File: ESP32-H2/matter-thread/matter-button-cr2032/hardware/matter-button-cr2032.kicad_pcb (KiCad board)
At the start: 2 copper layers, 30 x 38 mm, 37 parts, among them Q1 DMG2305UX, SW1 PTS810, U1 ESP32-H2-WROOM-02C-H4S, U2 TPS63900DSKR

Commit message: matter-button-cr2032: JLCPCB Basic parts and LCSC part numbers
Every assembled part now carries an LCSC part number (schematic field,
footprint field, BOM). Common parts moved to the JLCPCB Basic library:
- Q1 AO3401A (C15127) instead of DMG2305UX, same SOT-23 pinout
- D1 KT-0603R (C2286), passives UNI-ROYAL / Samsung Basic parts
- R3 (CFG3) 0 ohm as the TI 3.3 V reference design: VO(1) = 1.8 V,
  unused because SEL is tied to VIN; R2 and R3 share one part
- R6 button pull-up 1 Mohm (same part as R9): 3.3 uA while pressed
Extended parts left: U2, L1 (DFE252012P-2R2M), C1/C2, R1 36.5k, SW1
(PTS810 SJM, 160 gf). U1 and BT1 are not stocked by LCSC: left out of
the JLCPCB BOM and CPL, hand soldered.

gen_pcb.py sync updates values and part fields on the routed board
without placement or routing. Copper and Gerbers are unchanged;
ERC 0, DRC 0 with schematic parity.

Co-Authored-By: Claude Opus 5.5 <noreply@anthropic.com>
Claude-Session: https://claude.ai/code/session_01R15P3zWK2KCijMWrCL7LHn
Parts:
- Q1: value DMG2305UX -> AO3401A
- R3: value 16.2k -> 0R
- R6: value 470k -> 1M

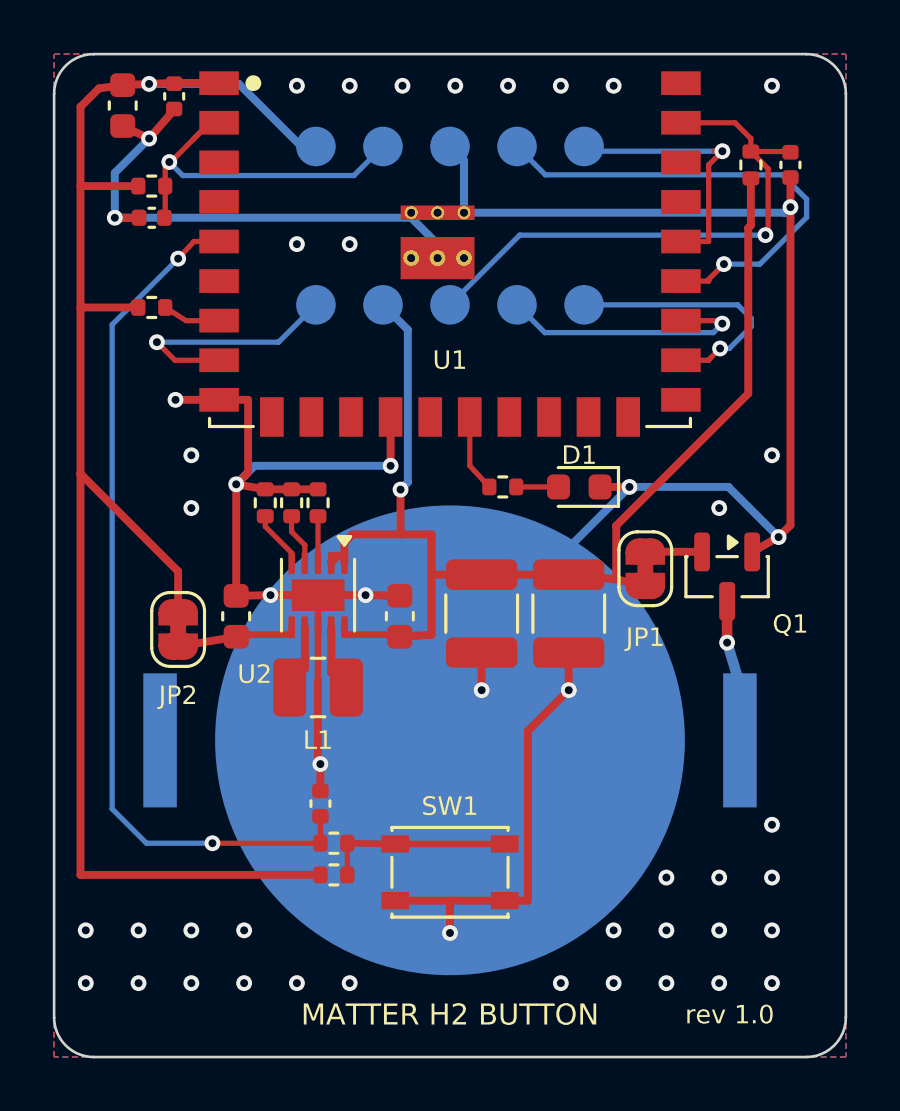
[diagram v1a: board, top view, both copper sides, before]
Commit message: matter-button-cr2032: compact 25 x 27 mm PCB
Same schematic, new layout: the CR2032 holder moves under the module and
the circuit, the board shrinks from 30 x 38 to 25 x 27 mm (41 % less area).
- the holder (23.2 mm between its tab ends) sets the width; the cell edge
  is now 6.5 mm from the antenna feed (was ~16 mm), the docs ask for an
  RSSI/LQI check and point to the previous layout as fallback
- bottom side: no copper in a ring around the cell edge (the + can), GND
  vias only inside the contact pad or outside the cell
- test pads stay on the bottom side under the module (2 x 5, 2.54 x 2.7 mm)
- gen_pcb.py: new placement and hand routes, coin-cell ring rule areas,
  duplicate segment cleanup, saving the board keeps the project file
ERC 0, DRC 0 with schematic parity.

Co-Authored-By: Claude Opus 5.5 <noreply@anthropic.com>
Claude-Session: https://claude.ai/code/session_01R15P3zWK2KCijMWrCL7LHn
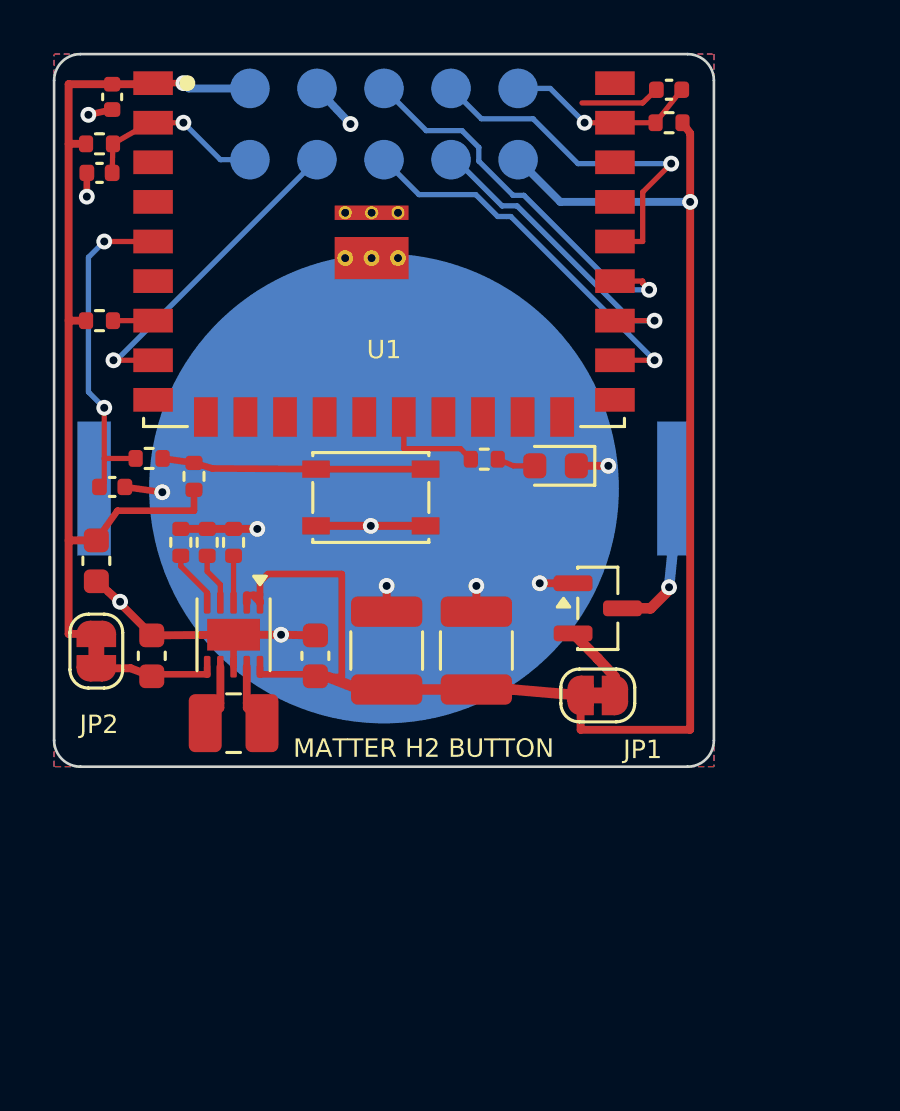
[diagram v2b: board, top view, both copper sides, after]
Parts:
- moved C5 17.3 mm to (101.6, 119.2)
- moved R7 16.2 mm to (103.6, 115.3)
- moved R6 16.0 mm to (105.3, 116.0), turned to 90 degrees
- moved SW1 14.5 mm to (112.0, 116.8)
- moved C8 14.4 mm to (102.2, 116.4), turned to 0 degrees
- moved BT1 9.86 mm to (112.5, 116.5)
- moved TP4 9.37 mm to (112.5, 104.0)
- moved TP10 8.60 mm to (117.6, 101.3)
- moved TP9 7.51 mm to (117.6, 104.0)
- moved C2 7.04 mm to (112.6, 122.6), turned to 90 degrees
- moved TP3 6.04 mm to (115.0, 104.0)
- moved TP6 5.50 mm to (110.0, 104.0)
- moved TP2 5.50 mm to (110.0, 101.3)
- moved TP7 5.50 mm to (112.5, 101.3)
- moved TP8 5.50 mm to (115.0, 101.3)
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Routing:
- net GND: track 137.8 -> 34.7 mm, vias 51 -> 12
- net +3V3: track 62.2 -> 36.3 mm
- net /BTN: track 33.2 -> 12.9 mm
- net /VBAT_SENSE: track 21.4 -> 6.69 mm
- net VBAT: track 47.8 -> 57.7 mm
- net /EN: track 13.9 -> 7.13 mm
- net /RXD0: track 10.1 -> 14.9 mm
- net /USB_DN: track 18.3 -> 15.0 mm
- net /BOOT: track 9.25 -> 12.4 mm
- net /BTN_SW: track 7.17 -> 10.0 mm
- net /USB_DP: track 11.2 -> 14.0 mm
- net /TXD0: track 9.97 -> 11.7 mm
- net /LED: track 2.94 -> 3.91 mm
- net /VBAT_Q: track 2.16 -> 2.99 mm
- net /LX2: track 1.59 -> 2.38 mm
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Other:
- board size 30 x 38 mm -> 25 x 27 mm
- board text removed: "CR2032 +"

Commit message: matter-button-cr2032: 29.8 x 23.9 mm PCB, under 30 x 30 mm with the antenna
Same schematic, new layout so the whole board including the module antenna
overhang fits in 30 x 30 mm (29.8 x 29.9 mm), no mounting holes.
- module at the top right edge, passives and the TPS63900 on its left,
  button in the middle, battery input and sense on the right
- the cell edge is now 3.4 mm from the antenna base (25 x 27 mm: 6.5 mm);
  the docs ask for an RSSI/LQI check and point to the earlier layouts
- test pads: 2 x 2 in each top corner, RX and VBAT right of the holder;
  every signal is routed in the script, so the route stage skips
  FreeRouting when only GND (the pours) is left
- silkscreen: "Thread Button" (top), "Made by Haxeko" (bottom), JP1 label
- place no longer leaves the project file rewritten with KiCad defaults
  (NewBoard writes it before the save), 3D renders in landscape
ERC 0, DRC 0 with schematic parity; BOM unchanged.

Co-Authored-By: Claude Opus 5.5 <noreply@anthropic.com>
Claude-Session: https://claude.ai/code/session_01R15P3zWK2KCijMWrCL7LHn
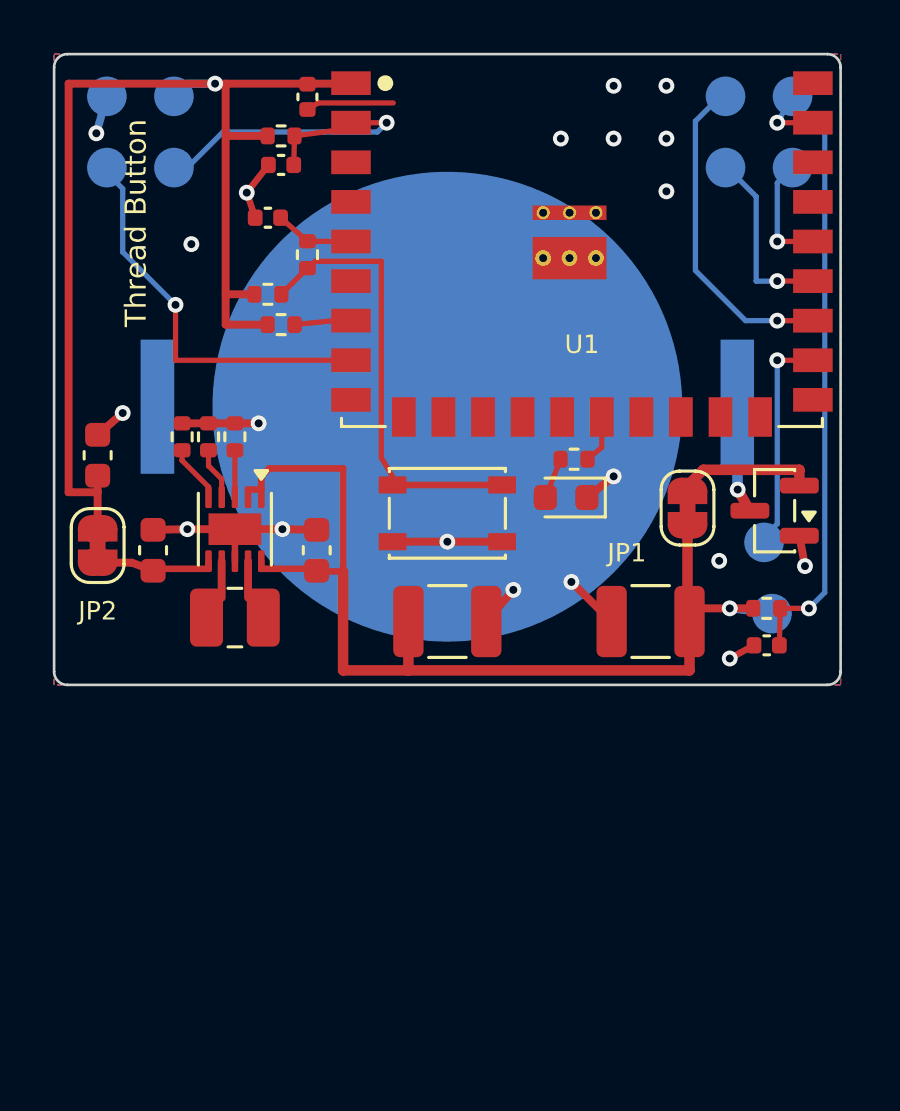
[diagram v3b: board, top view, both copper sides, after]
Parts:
- moved C9 21.4 mm to (127.0, 122.4)
- moved TP4 20.4 mm to (126.9, 118.5)
- moved TP9 19.7 mm to (127.2, 121.2)
- moved R9 18.8 mm to (127.0, 121.0), turned to 0 degrees
- moved TP7 13.3 mm to (125.4, 104.3)
- moved TP8 13.3 mm to (128.0, 104.3)
- moved C8 11.8 mm to (108.1, 106.2), turned to 180 degrees
- moved TP3 10.7 mm to (125.4, 101.6)
- moved TP10 10.4 mm to (128.0, 101.6)
- moved R7 9.78 mm to (109.6, 107.6), turned to 90 degrees
- moved TP2 7.97 mm to (102.0, 101.6)
- moved TP6 7.97 mm to (102.0, 104.3)
- moved JP1 7.87 mm to (124.0, 117.2), turned to -90 degrees
- moved Q1 7.65 mm to (127.3, 117.3), turned to 180 degrees
- moved U1 7.50 mm to (120.0, 104.0)
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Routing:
- net VBAT: track 57.7 -> 34.9 mm
- net /VBAT_SENSE: track 6.69 -> 23.9 mm, vias 1 -> 2
- net /BTN: track 12.9 -> 2.35 mm, vias 2 -> 0
- net /USB_DP: track 14.0 -> 3.74 mm
- net /USB_DN: track 15.0 -> 6.26 mm
- net /RXD0: track 14.9 -> 7.18 mm
- net +3V3: track 36.3 -> 43.3 mm
- net /BTN_SW: track 10.0 -> 16.7 mm
- net GND: track 34.7 -> 30.1 mm, vias 12 -> 20
- net /EN: track 7.13 -> 11.3 mm
- net /BAT+: track 5.91 -> 1.82 mm
- net /LED: track 3.91 -> 1.20 mm
- net /VBAT_Q: track 2.99 -> 5.09 mm
- net /BOOT: track 12.4 -> 13.9 mm
- net /LX2: track 2.38 -> 1.39 mm
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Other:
- board size 25 x 27 mm -> 29.8 x 23.9 mm
- board text added: "Made by Haxeko"
- board text added: "Thread Button"
- board text removed: "MATTER H2 BUTTON"
